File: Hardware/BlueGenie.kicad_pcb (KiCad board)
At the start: 2 copper layers, 26.4 x 40.4 mm, 11 parts, among them J1 Conn_01x08_Female, J2 Screw_Terminal_01x02, J3 MCP2515_Connector_01x07_Female, J4 Conn_01x08_Female

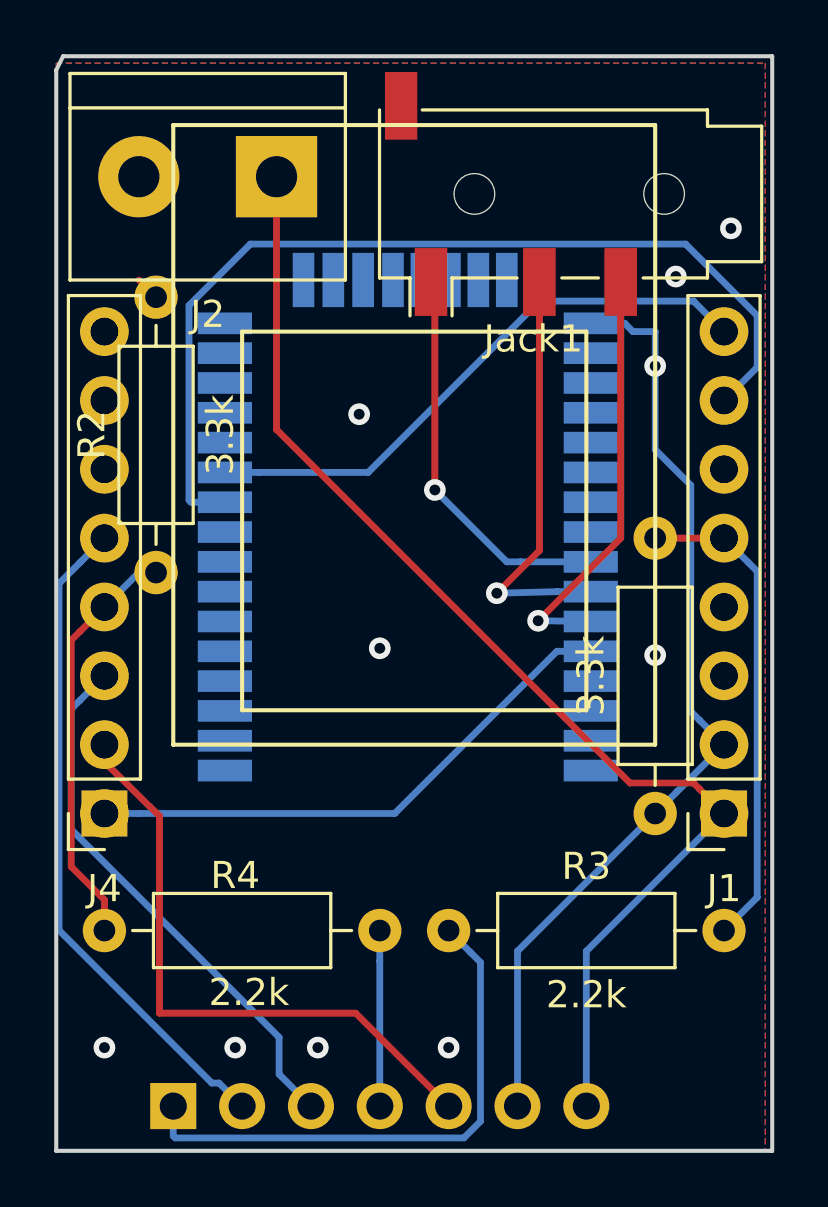
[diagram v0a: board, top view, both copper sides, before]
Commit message: Shorted pin 12 fixed
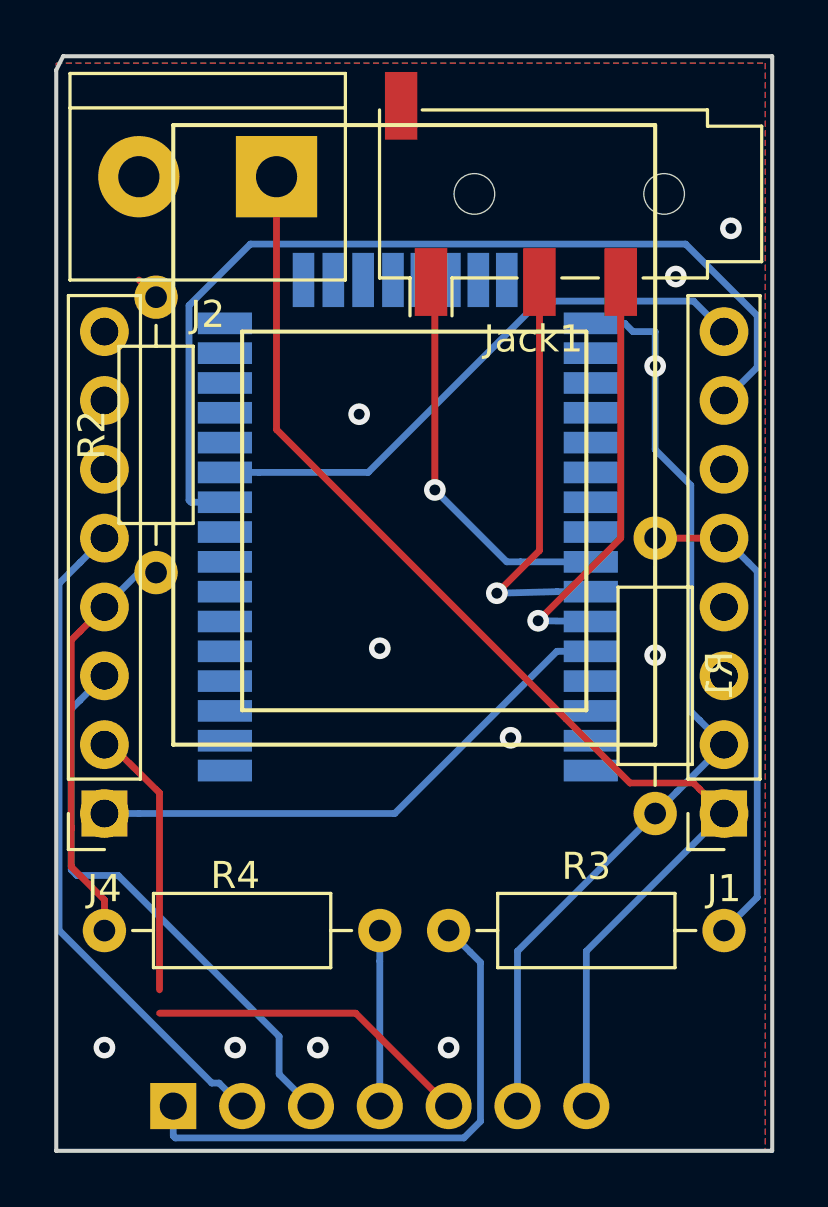
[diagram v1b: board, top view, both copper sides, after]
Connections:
- BK3254 pad 25: Net-(BK3254-Pad25) -> GND
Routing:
- net /MOSI: track 20.0 -> 21.0 mm
- net GND: vias 10 -> 11
